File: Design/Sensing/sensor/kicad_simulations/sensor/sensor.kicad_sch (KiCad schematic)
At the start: 42 parts, among them J1 Conn_01x02_Pin, J10 Conn_01x02_Pin, J11 Conn_01x02_Pin, J12 Conn_01x02_Pin, J13 Conn_01x02_Pin, J14 Conn_01x01_Pin, J15 Conn_01x01_Pin, J16 Conn_01x02_Pin, J17 Conn_01x02_Pin, J2 Conn_01x02_Pin, J3 Conn_02x14_Counter_Clockwise, J4 Conn_01x01_Pin, J5 L_S_B, J6 Conn_01x01_Pin, J7 Conn_01x02_Pin, J8 Conn_01x02_Pin, J9 Conn_01x02_Pin, Q1 MMBT5551L, Q2 MMBT5551L, Q3 MMBT5551L, U1 LM324, U2 TSSP58038, U3 TSSP58038, U4 TSSP58038

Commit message: Routed correct design
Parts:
- removed D2, D4, D6: TSAL4400, LED_THT:LED_D3.0mm_Horizontal_O1.27mm_Z2.0mm_IRBlack, symbol LED:TSAL4400
- removed J4: Conn_01x01_Pin, Connector_PinHeader_2.54mm:PinHeader_1x01_P2.54mm_Vertical, symbol Connector:Conn_01x01_Pin
- R2, R5, R6: value 18 -> 22
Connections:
- net 5V is gone; now on net 3V3: D1.2 (A), D3.2 (A), D5.2 (A), J1.1 (Pin_1), J10.1 (Pin_1), J8.1 (Pin_1)
- net at R5.2: now also D3.1 (K)
- net at D1.1 (K): now also R2.2
- net at D5.1 (K): now also R6.2

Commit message: IR change
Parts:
- removed D1, D3, D5: TSAL4400, LED_THT:LED_D3.0mm_Horizontal_O1.27mm_Z2.0mm_IRBlack, symbol LED:TSAL4400
- added D1, D2, D3: IR204A, LED_THT:LED_D3.0mm_Horizontal_O1.27mm_Z2.0mm_IRBlack, symbol LED:IR204A
- R1, R2, R3, R5, R6: footprint Resistor_SMD:R_1206_3216Metric -> Resistor_SMD:R_0805_2012Metric
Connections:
- net 3V3: now also D1.2 (A), D2.2 (A), D3.2 (A)
- net at R5.2: now also D1.1 (K)
- net at R2.2: now also D2.1 (K)
- net at R6.2: now also D3.1 (K)
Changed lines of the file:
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@@
 			)
 		)
-		(property "Footprint" "Resistor_SMD:R_1206_3216Metric"
+		(property "Footprint" "Resistor_SMD:R_0805_2012Metric"
 			(at 213.868 74.93 90)
 			(effects
@@
 	)
 	(symbol
-		(lib_id "LED:TSAL4400")
-		(at 60.96 54.61 90)
-		(unit 1)
-		(exclude_from_sim no)
-		(in_bom yes)
-		(on_board yes)
-		(dnp no)
-		(fields_autoplaced yes)
-		(property "Reference" "D1"
-			(at 63.5 54.4829 90)
-			(effects
-				(font
-					(size 1.27 1.27)
-				)
-				(justify right)
-			)
-		)
-		(property "Value" "TSAL4400"
-			(at 63.5 57.0229 90)
-			(effects
-				(font
-					(size 1.27 1.27)
-				)
-				(justify right)
-			)
-		)
-		(property "Footprint" "LED_THT:LED_D3.0mm_Horizontal_O1.27mm_Z2.0mm_IRBlack"
-			(at 56.515 54.61 0)
-			(effects
-				(font
-					(size 1.27 1.27)
-				)
-				(hide yes)
-			)
-		)
-		(property "Datasheet" "http://www.vishay.com/docs/81006/tsal4400.pdf"
-			(at 60.96 55.88 0)
-			(effects
-				(font
-					(size 1.27 1.27)
-				)
-				(hide yes)
-			)
-		)
-		(property "Description" "Infrared LED , 3mm LED package"
-			(at 60.96 54.61 0)
-			(effects
-				(font
-					(size 1.27 1.27)
-				)
-				(hide yes)
-			)
-		)
-		(pin "1"
-		)
-		(pin "2"
-		)
-		(instances
-			(project "sensor"
-				(path "/fddf1a24-418d-41c5-aa43-003ad0e16f35"
-					(reference "D1")
-					(unit 1)
-				)
-			)
-		)
-	)
-	(symbol
 		(lib_id "Connector:Conn_01x02_Pin")
 		(at 195.58 73.66 0)
@@
 	)
 	(symbol
-		(lib_id "LED:TSAL4400")
-		(at 213.36 149.86 90)
-		(unit 1)
-		(exclude_from_sim no)
-		(in_bom yes)
-		(on_board yes)
-		(dnp no)
-		(fields_autoplaced yes)
-		(property "Reference" "D5"
-			(at 215.9 149.7329 90)
-			(effects
-				(font
-					(size 1.27 1.27)
-				)
-				(justify right)
-			)
-		)
-		(property "Value" "TSAL4400"
-			(at 215.9 152.2729 90)
-			(effects
-				(font
-					(size 1.27 1.27)
-				)
-				(justify right)
-			)
-		)
-		(property "Footprint" "LED_THT:LED_D3.0mm_Horizontal_O1.27mm_Z2.0mm_IRBlack"
-			(at 208.915 149.86 0)
-			(effects
-				(font
-					(size 1.27 1.27)
-				)
-				(hide yes)
-			)
-		)
-		(property "Datasheet" "http://www.vishay.com/docs/81006/tsal4400.pdf"
-			(at 213.36 151.13 0)
-			(effects
-				(font
-					(size 1.27 1.27)
-				)
-				(hide yes)
-			)
-		)
-		(property "Description" "Infrared LED , 3mm LED package"
-			(at 213.36 149.86 0)
-			(effects
-				(font
-					(size 1.27 1.27)
-				)
-				(hide yes)
-			)
-		)
-		(pin "1"
-		)
-		(pin "2"
-		)
-		(instances
-			(project "sensor"
-				(path "/fddf1a24-418d-41c5-aa43-003ad0e16f35"
-					(reference "D5")
-					(unit 1)
-				)
-			)
-		)
-	)
-	(symbol
 		(lib_id "Amplifier_Operational:LM324")
 		(at 342.9 90.17 0)
@@
 			)
 		)
-		(property "Footprint" "Resistor_SMD:R_1206_3216Metric"
+		(property "Footprint" "Resistor_SMD:R_0805_2012Metric"
 			(at 62.738 73.66 90)
 			(effects
@@
 			)
 		)
-		(property "Footprint" "Resistor_SMD:R_1206_3216Metric"
+		(property "Footprint" "Resistor_SMD:R_0805_2012Metric"
 			(at 43.18 84.582 90)
 			(effects
@@
 	)
 	(symbol
+		(lib_id "LED:IR204A")
+		(at 60.96 54.61 90)
+		(unit 1)
+		(exclude_from_sim no)
+		(in_bom yes)
+		(on_board yes)
+		(dnp no)
+		(fields_autoplaced yes)
+		(property "Reference" "D2"
+			(at 63.5 54.4829 90)
+			(effects
+				(font
+					(size 1.27 1.27)
+				)
+				(justify right)
+			)
+		)
+		(property "Value" "IR204A"
+			(at 63.5 57.0229 90)
+			(effects
+				(font
+					(size 1.27 1.27)
+				)
+				(justify right)
+			)
+		)
+		(property "Footprint" "LED_THT:LED_D3.0mm_Horizontal_O1.27mm_Z2.0mm_IRBlack"
+			(at 56.515 54.61 0)
+			(effects
+				(font
+					(size 1.27 1.27)
+				)
+				(hide yes)
+			)
+		)
+		(property "Datasheet" "http://www.everlight.com/file/ProductFile/IR204-A.pdf"
+			(at 60.96 55.88 0)
+			(effects
+				(font
+					(size 1.27 1.27)
+				)
+				(hide yes)
+			)
+		)
+		(property "Description" "Infrared LED , 3mm LED package"
+			(at 60.96 54.61 0)
+			(effects
+				(font
+					(size 1.27 1.27)
+				)
+				(hide yes)
+			)
+		)
+		(pin "1"
+		)
+		(pin "2"
+		)
+		(instances
+			(project "sensor"
+				(path "/fddf1a24-418d-41c5-aa43-003ad0e16f35"
+					(reference "D2")
+					(unit 1)
+				)
+			)
+		)
+	)
+	(symbol
 		(lib_id "power:GND")
 		(at 236.22 170.18 0)
@@
 			)
 		)
-		(property "Footprint" "Resistor_SMD:R_1206_3216Metric"
+		(property "Footprint" "Resistor_SMD:R_0805_2012Metric"
 			(at 194.31 85.852 90)
 			(effects
@@
 	)
 	(symbol
+		(lib_id "LED:IR204A")
+		(at 212.09 55.88 90)
+		(unit 1)
+		(exclude_from_sim no)
+		(in_bom yes)
+		(on_board yes)
+		(dnp no)
+		(fields_autoplaced yes)
+		(property "Reference" "D1"
+			(at 214.63 55.7529 90)
+			(effects
+				(font
+					(size 1.27 1.27)
+				)
+				(justify right)
+			)
+		)
+		(property "Value" "IR204A"
+			(at 214.63 58.2929 90)
+			(effects
+				(font
+					(size 1.27 1.27)
+				)
+				(justify right)
+			)
+		)
+		(property "Footprint" "LED_THT:LED_D3.0mm_Horizontal_O1.27mm_Z2.0mm_IRBlack"
+			(at 207.645 55.88 0)
+			(effects
+				(font
+					(size 1.27 1.27)
+				)
+				(hide yes)
+			)
+		)
+		(property "Datasheet" "http://www.everlight.com/file/ProductFile/IR204-A.pdf"
+			(at 212.09 57.15 0)
+			(effects
+				(font
+					(size 1.27 1.27)
+				)
+				(hide yes)
+			)
+		)
+		(property "Description" "Infrared LED , 3mm LED package"
+			(at 212.09 55.88 0)
+			(effects
+				(font
+					(size 1.27 1.27)
+				)
+				(hide yes)
+			)
+		)
+		(pin "1"
+		)
+		(pin "2"
+		)
+		(instances
+			(project "sensor"
+				(path "/fddf1a24-418d-41c5-aa43-003ad0e16f35"
+					(reference "D1")
+					(unit 1)
+				)
+			)
+		)
+	)
+	(symbol
 		(lib_id "Device:R")
 		(at 213.36 168.91 180)
@@
 			)
 		)
-		(property "Footprint" "Resistor_SMD:R_1206_3216Metric"
+		(property "Footprint" "Resistor_SMD:R_0805_2012Metric"
 			(at 215.138 168.91 90)
 			(effects
@@
 	)
 	(symbol
-		(lib_id "LED:TSAL4400")
-		(at 212.09 55.88 90)
-		(unit 1)
-		(exclude_from_sim no)
-		(in_bom yes)
-		(on_board yes)
-		(dnp no)
-		(fields_autoplaced yes)
-		(property "Reference" "D3"
-			(at 214.63 55.7529 90)
-			(effects
-				(font
-					(size 1.27 1.27)
-				)
-				(justify right)
-			)
-		)
-		(property "Value" "TSAL4400"
-			(at 214.63 58.2929 90)
-			(effects
-				(font
-					(size 1.27 1.27)
-				)
-				(justify right)
-			)
-		)
-		(property "Footprint" "LED_THT:LED_D3.0mm_Horizontal_O1.27mm_Z2.0mm_IRBlack"
-			(at 207.645 55.88 0)
-			(effects
-				(font
-					(size 1.27 1.27)
-				)
-				(hide yes)
-			)
-		)
-		(property "Datasheet" "http://www.vishay.com/docs/81006/tsal4400.pdf"
-			(at 212.09 57.15 0)
-			(effects
-				(font
-					(size 1.27 1.27)
-				)
-				(hide yes)
-			)
-		)
-		(property "Description" "Infrared LED , 3mm LED package"
-			(at 212.09 55.88 0)
-			(effects
-				(font
-					(size 1.27 1.27)
-				)
-				(hide yes)
-			)
-		)
-		(pin "1"
-		)
-		(pin "2"
-		)
-		(instances
-			(project "sensor"
-				(path "/fddf1a24-418d-41c5-aa43-003ad0e16f35"
-					(reference "D3")
-					(unit 1)
-				)
-			)
-		)
-	)
-	(symbol
 		(lib_id "Device:R")
 		(at 195.58 181.61 270)
@@
 					(unit 1)
 				)
+			)
+		)
+	)
+	(symbol
+		(lib_id "LED:IR204A")
+		(at 213.36 149.86 90)
+		(unit 1)
+		(exclude_from_sim no)
+		(in_bom yes)
+		(on_board yes)
+		(dnp no)
+		(fields_autoplaced yes)
+		(property "Reference" "D3"
+			(at 215.9 149.7329 90)
+			(effects
+				(font
+					(size 1.27 1.27)
+				)
+				(justify right)
+			)
+		)
+		(property "Value" "IR204A"
+			(at 215.9 152.2729 90)
+			(effects
+				(font
+					(size 1.27 1.27)
+				)
+				(justify right)
+			)
+		)
+		(property "Footprint" "LED_THT:LED_D3.0mm_Horizontal_O1.27mm_Z2.0mm_IRBlack"
+			(at 208.915 149.86 0)
+			(effects
+				(font
+					(size 1.27 1.27)
+				)
+				(hide yes)
+			)
+		)
+		(property "Datasheet" "http://www.everlight.com/file/ProductFile/IR204-A.pdf"
+			(at 213.36 151.13 0)
+			(effects
+				(font
+					(size 1.27 1.27)
+				)
+				(hide yes)
+			)
+		)
+		(property "Description" "Infrared LED , 3mm LED package"
+			(at 213.36 149.86 0)
+			(effects
+				(font
+					(size 1.27 1.27)
+				)
+				(hide yes)
+			)
+		)
+		(pin "1"
+		)
+		(pin "2"
+		)
+		(instances
+			(project "sensor"
+				(path "/fddf1a24-418d-41c5-aa43-003ad0e16f35"
+					(reference "D3")
+					(unit 1)
+				)

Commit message: Gerber files done
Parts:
- R4: footprint Resistor_SMD:R_1206_3216Metric -> Resistor_SMD:R_0805_2012Metric
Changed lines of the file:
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@@
 			)
 		)
-		(property "Footprint" "Resistor_SMD:R_1206_3216Metric"
+		(property "Footprint" "Resistor_SMD:R_0805_2012Metric"
 			(at 195.58 179.832 90)
 			(effects

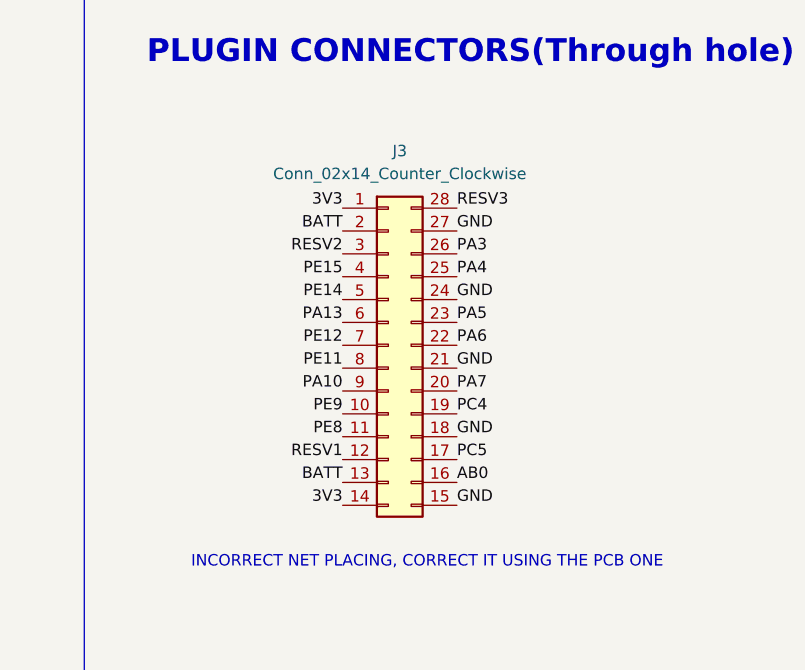
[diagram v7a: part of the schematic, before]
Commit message: ensured that net names in the connectors matches the label in th project
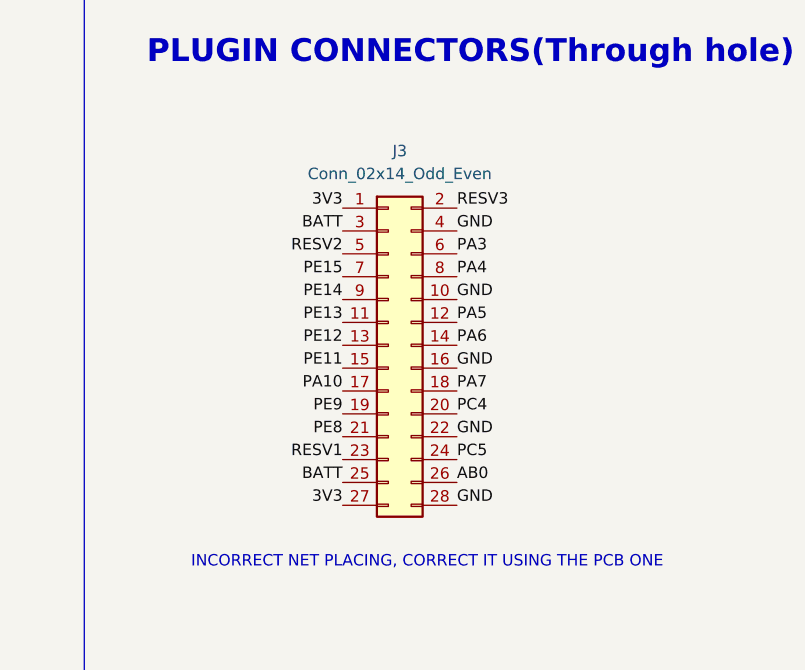
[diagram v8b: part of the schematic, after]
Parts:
- removed J3: Conn_02x14_Counter_Clockwise, Connector_PinSocket_2.54mm:PinSocket_2x14_P2.54mm_Vertical, symbol Connector_Generic:Conn_02x14_Counter_Clockwise
- added J3: Conn_02x14_Odd_Even, Connector_PinHeader_2.54mm:PinHeader_2x14_P2.54mm_Vertical, symbol Connector_Generic:Conn_02x14_Odd_Even
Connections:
- net 3V3: now also J3.1 (Pin_1), J3.27 (Pin_27)
- net AB0: now also J3.26 (Pin_26)
- net BATT: now also J3.25 (Pin_25), J3.3 (Pin_3)
- net GND: now also J3.10 (Pin_10), J3.16 (Pin_16), J3.22 (Pin_22), J3.28 (Pin_28), J3.4 (Pin_4)
- net PA10: now also J3.17 (Pin_17)
- net PA3: now also J3.6 (Pin_6)
- net PA4: now also J3.8 (Pin_8)
- net PA5: now also J3.12 (Pin_12)
- net PA6: now also J3.14 (Pin_14)
- net PA7: now also J3.18 (Pin_18)
- net PC4: now also J3.20 (Pin_20)
- net PC5: now also J3.24 (Pin_24)
- net PE11: now also J3.15 (Pin_15)
- net PE12: now also J3.13 (Pin_13)
- net PE14: now also J3.9 (Pin_9)
- net PE15: now also J3.7 (Pin_7)
- net PE8: now also J3.21 (Pin_21)
- net PE9: now also J3.19 (Pin_19)
- net RESV1: now also J3.23 (Pin_23)
- net RESV2: now also J3.5 (Pin_5)
- net RESV3: now also J3.2 (Pin_2)
- new net PE13: J3.11 (Pin_11)
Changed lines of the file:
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@@
 		)
 	)
-	(label "PA13"
+	(label "PE13"
 		(at 66.04 176.53 180)
 		(fields_autoplaced yes)
@@
 	)
 	(symbol
+		(lib_id "Connector_Generic:Conn_02x14_Odd_Even")
+		(at 71.12 179.07 0)
+		(unit 1)
+		(exclude_from_sim no)
+		(in_bom yes)
+		(on_board yes)
+		(dnp no)
+		(fields_autoplaced yes)
+		(property "Reference" "J3"
+			(at 72.39 157.48 0)
+			(effects
+				(font
+					(size 1.27 1.27)
+				)
+			)
+		)
+		(property "Value" "Conn_02x14_Odd_Even"
+			(at 72.39 160.02 0)
+			(effects
+				(font
+					(size 1.27 1.27)
+				)
+			)
+		)
+		(property "Footprint" "Connector_PinHeader_2.54mm:PinHeader_2x14_P2.54mm_Vertical"
+			(at 71.12 179.07 0)
+			(effects
+				(font
+					(size 1.27 1.27)
+				)
+				(hide yes)
+			)
+		)
+		(property "Datasheet" "~"
+			(at 71.12 179.07 0)
+			(effects
+				(font
+					(size 1.27 1.27)
+				)
+				(hide yes)
+			)
+		)
+		(property "Description" "Generic connector, double row, 02x14, odd/even pin numbering scheme (row 1 odd numbers, row 2 even numbers), script generated (kicad-library-utils/schlib/autogen/connector/)"
+			(at 71.12 179.07 0)
+			(effects
+				(font
+					(size 1.27 1.27)
+				)
+				(hide yes)
+			)
+		)
+		(pin "26"
+		)
+		(pin "19"
+		)
+		(pin "20"
+		)
+		(pin "22"
+		)
+		(pin "25"
+		)
+		(pin "3"
+		)
+		(pin "11"
+		)
+		(pin "13"
+		)
+		(pin "14"
+		)
+		(pin "2"
+		)
+		(pin "16"
+		)
+		(pin "5"
+		)
+		(pin "12"
+		)
+		(pin "21"
+		)
+		(pin "27"
+		)
+		(pin "15"
+		)
+		(pin "18"
+		)
+		(pin "1"
+		)
+		(pin "6"
+		)
+		(pin "24"
+		)
+		(pin "7"
+		)
+		(pin "4"
+		)
+		(pin "8"
+		)
+		(pin "17"
+		)
+		(pin "28"
+		)
+		(pin "23"
+		)
+		(pin "9"
+		)
+		(pin "10"
+		)
+		(instances
+			(project "sensor"
+				(path "/fddf1a24-418d-41c5-aa43-003ad0e16f35"
+					(reference "J3")
+					(unit 1)
+				)
+			)
+		)
+	)
+	(symbol
 		(lib_id "Transistor_BJT:MMBT5551L")
 		(at 58.42 86.36 0)
@@
 					(unit 1)
 				)
-			)
-		)
-	)
-	(symbol
-		(lib_id "Connector_Generic:Conn_02x14_Counter_Clockwise")
-		(at 71.12 179.07 0)
-		(unit 1)
-		(exclude_from_sim no)
-		(in_bom yes)
-		(on_board yes)
-		(dnp no)
-		(fields_autoplaced yes)
-		(property "Reference" "J3"
-			(at 72.39 157.48 0)
-			(effects
-				(font
-					(size 1.27 1.27)
-				)
-			)
-		)
-		(property "Value" "Conn_02x14_Counter_Clockwise"
-			(at 72.39 160.02 0)
-			(effects
-				(font
-					(size 1.27 1.27)
-				)
-			)
-		)
-		(property "Footprint" "Connector_PinSocket_2.54mm:PinSocket_2x14_P2.54mm_Vertical"
-			(at 71.12 179.07 0)
-			(effects
-				(font
-					(size 1.27 1.27)
-				)
-				(hide yes)
-			)
-		)
-		(property "Datasheet" "~"
-			(at 71.12 179.07 0)
-			(effects
-				(font
-					(size 1.27 1.27)
-				)
-				(hide yes)
-			)
-		)
-		(property "Description" "Generic connector, double row, 02x14, counter clockwise pin numbering scheme (similar to DIP package numbering), script generated (kicad-library-utils/schlib/autogen/connector/)"
-			(at 71.12 179.07 0)
-			(effects
-				(font
-					(size 1.27 1.27)
-				)
-				(hide yes)
-			)
-		)
-		(pin "10"
-		)
-		(pin "27"
-		)
-		(pin "25"
-		)
-		(pin "28"
-		)
-		(pin "15"
-		)
-		(pin "16"
-		)
-		(pin "21"
-		)
-		(pin "23"
-		)
-		(pin "12"
-		)
-		(pin "4"
-		)
-		(pin "19"
-		)
-		(pin "22"
-		)
-		(pin "5"
-		)
-		(pin "8"
-		)
-		(pin "3"
-		)
-		(pin "14"
-		)
-		(pin "1"
-		)
-		(pin "24"
-		)
-		(pin "13"
-		)
-		(pin "7"
-		)
-		(pin "6"
-		)
-		(pin "20"
-		)
-		(pin "11"
-		)
-		(pin "2"
-		)
-		(pin "9"
-		)
-		(pin "18"
-		)
-		(pin "17"
-		)
-		(pin "26"
-		)
-		(instances
-			(project "sensor"
-				(path "/fddf1a24-418d-41c5-aa43-003ad0e16f35"
-					(reference "J3")
-					(unit 1)
-				)
